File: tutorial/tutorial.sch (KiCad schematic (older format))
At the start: 9 parts

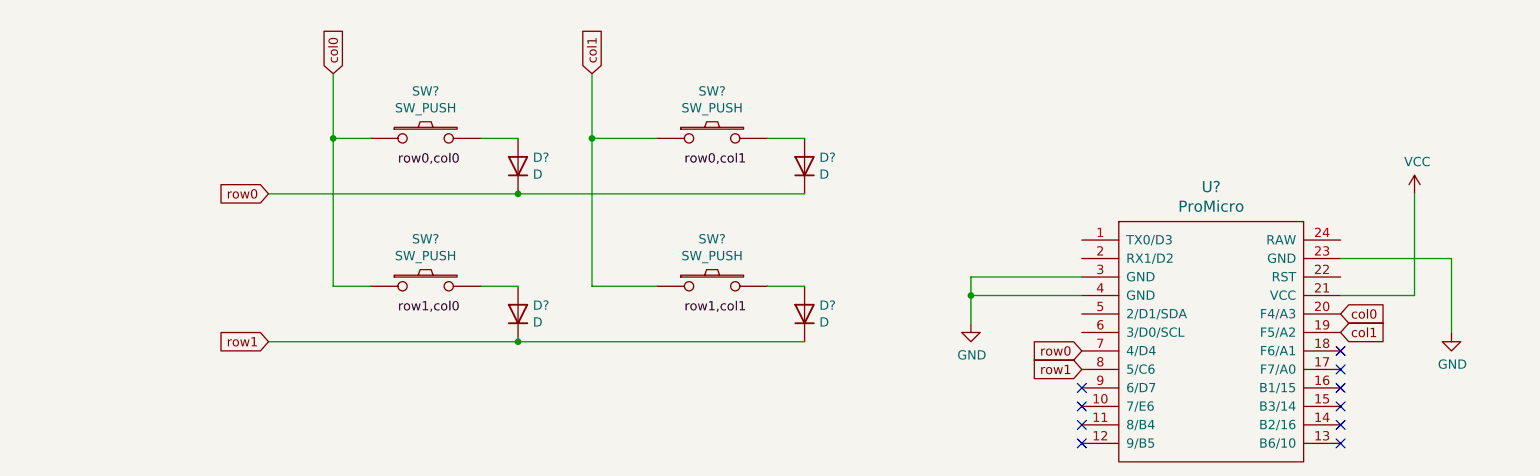
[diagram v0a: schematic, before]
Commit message: [update] リセットスイッチの配置
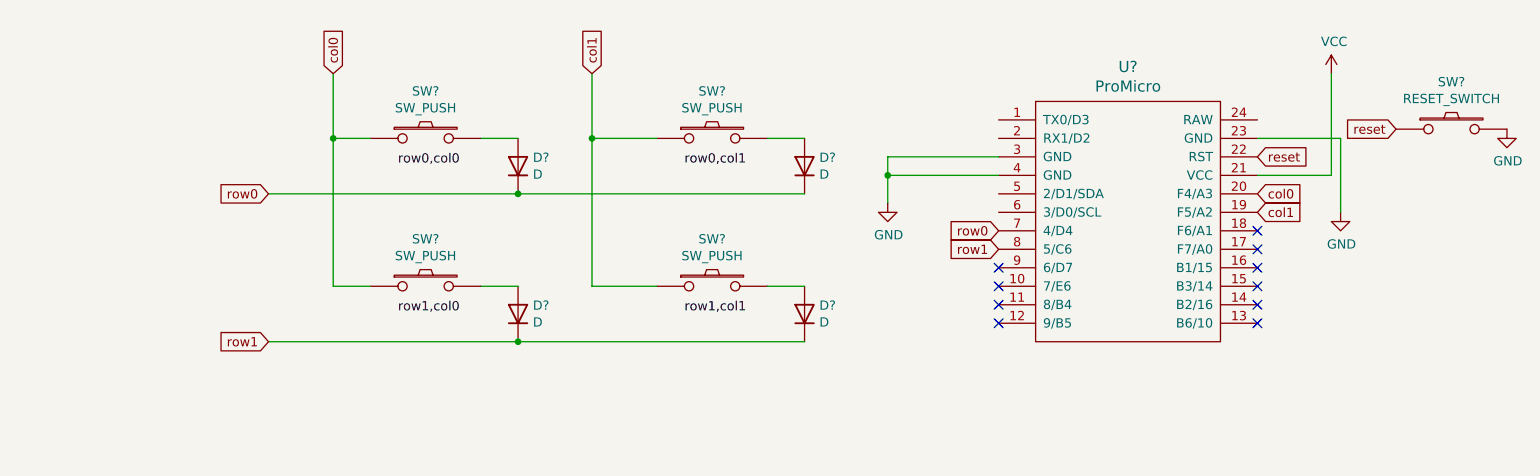
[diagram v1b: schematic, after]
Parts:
- added SW?: RESET_SWITCH, symbol kbd:SW_PUSH
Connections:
- net GND: now also SW?.2
- net reset: now reaches U?.22 (RST)
- net reset: now also SW?.1
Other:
- moved on the sheet: U?
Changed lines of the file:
@@
-$Comp
-L power:GND #PWR?
-U 1 1 62F696F1
-P 10650 2300
-F 0 "#PWR?" H 10650 2050 50  0001 C CNN
-F 1 "GND" H 10655 2127 50  0000 C CNN
-F 2 "" H 10650 2300 50  0001 C CNN
-F 3 "" H 10650 2300 50  0001 C CNN
-	1    10650 2300
-	1    0    0    -1
-$EndComp
 $Comp
 L power:GND #PWR?
 U 1 1 62F6A3B7
-P 8050 2250
-F 0 "#PWR?" H 8050 2000 50  0001 C CNN
-F 1 "GND" H 8055 2077 50  0000 C CNN
-F 2 "" H 8050 2250 50  0001 C CNN
-F 3 "" H 8050 2250 50  0001 C CNN
-	1    8050 2250
+P 7600 1600
+F 0 "#PWR?" H 7600 1350 50  0001 C CNN
+F 1 "GND" H 7605 1427 50  0000 C CNN
+F 2 "" H 7600 1600 50  0001 C CNN
+F 3 "" H 7600 1600 50  0001 C CNN
+	1    7600 1600
 	1    0    0    -1
 $EndComp
@@
 L power:VCC #PWR?
 U 1 1 62F6AAB7
-P 10450 1550
-F 0 "#PWR?" H 10450 1400 50  0001 C CNN
-F 1 "VCC" H 10465 1723 50  0000 C CNN
-F 2 "" H 10450 1550 50  0001 C CNN
-F 3 "" H 10450 1550 50  0001 C CNN
-	1    10450 1550
-	1    0    0    -1
-$EndComp
-Wire Wire Line
-	10050 2100 10450 2100
-Wire Wire Line
-	10450 2100 10450 1550
+P 10000 900
+F 0 "#PWR?" H 10000 750 50  0001 C CNN
+F 1 "VCC" H 10015 1073 50  0000 C CNN
+F 2 "" H 10000 900 50  0001 C CNN
+F 3 "" H 10000 900 50  0001 C CNN
+	1    10000 900
+	1    0    0    -1
+$EndComp
+Wire Wire Line
+	9600 1450 10000 1450
+Wire Wire Line
+	10000 1450 10000 900
 $Comp
 L kbd:ProMicro U?
 U 1 1 62F683C9
-P 9350 2350
-F 0 "U?" H 9350 3187 60  0000 C CNN
-F 1 "ProMicro" H 9350 3081 60  0000 C CNN
-F 2 "" H 9450 1300 60  0000 C CNN
-F 3 "" H 9450 1300 60  0000 C CNN
-	1    9350 2350
-	1    0    0    -1
-$EndComp
-Wire Wire Line
-	10650 2300 10650 1900
-Wire Wire Line
-	10650 1900 10050 1900
-Wire Wire Line
-	8650 2000 8050 2000
-Wire Wire Line
-	8050 2000 8050 2100
-Wire Wire Line
-	8650 2100 8050 2100
-Connection ~ 8050 2100
-Wire Wire Line
-	8050 2100 8050 2250
+P 8900 1700
+F 0 "U?" H 8900 2537 60  0000 C CNN
+F 1 "ProMicro" H 8900 2431 60  0000 C CNN
+F 2 "" H 9000 650 60  0000 C CNN
+F 3 "" H 9000 650 60  0000 C CNN
+	1    8900 1700
+	1    0    0    -1
+$EndComp
+Wire Wire Line
+	10050 1250 9600 1250
+Wire Wire Line
+	8200 1350 7600 1350
+Wire Wire Line
+	7600 1350 7600 1450
+Wire Wire Line
+	8200 1450 7600 1450
+Connection ~ 7600 1450
+Wire Wire Line
+	7600 1450 7600 1600
 $Comp
 L kbd:SW_PUSH SW?
@@
 Text GLabel 4250 2350 0    50   Input ~ 0
 row1
-Text GLabel 10050 2200 2    50   Input ~ 0
+Text GLabel 9600 1550 2    50   Input ~ 0
 col0
-Text GLabel 10050 2300 2    50   Input ~ 0
+Text GLabel 9600 1650 2    50   Input ~ 0
 col1
-Text GLabel 8650 2400 0    50   Input ~ 0
+Text GLabel 8200 1750 0    50   Input ~ 0
 row0
-Text GLabel 8650 2500 0    50   Input ~ 0
+Text GLabel 8200 1850 0    50   Input ~ 0
 row1
-NoConn ~ 10050 2400
-NoConn ~ 10050 2500
-NoConn ~ 10050 2600
-NoConn ~ 10050 2700
-NoConn ~ 10050 2800
-NoConn ~ 10050 2900
-NoConn ~ 8650 2600
-NoConn ~ 8650 2700
-NoConn ~ 8650 2800
-NoConn ~ 8650 2900
+NoConn ~ 9600 1750
+NoConn ~ 9600 1850
+NoConn ~ 9600 1950
+NoConn ~ 9600 2050
+NoConn ~ 9600 2150
+NoConn ~ 9600 2250
+NoConn ~ 8200 1950
+NoConn ~ 8200 2050
+NoConn ~ 8200 2150
+NoConn ~ 8200 2250
+$Comp
+L kbd:SW_PUSH SW?
+U 1 1 62F85B25
+P 10650 1200
+F 0 "SW?" H 10650 1455 50  0000 C CNN
+F 1 "RESET_SWITCH" H 10650 1364 50  0000 C CNN
+F 2 "" H 10650 1200 50  0000 C CNN
+F 3 "" H 10650 1200 50  0000 C CNN
+	1    10650 1200
+	1    0    0    -1
+$EndComp
+$Comp
+L power:GND #PWR?
+U 1 1 62F880C9
+P 10950 1200
+F 0 "#PWR?" H 10950 950 50  0001 C CNN
+F 1 "GND" H 10955 1027 50  0000 C CNN
+F 2 "" H 10950 1200 50  0001 C CNN
+F 3 "" H 10950 1200 50  0001 C CNN
+	1    10950 1200
+	1    0    0    -1
+$EndComp
+Text GLabel 10350 1200 0    50   Input ~ 0
+reset
+Wire Wire Line
+	10050 1650 10050 1250
+$Comp
+L power:GND #PWR?
+U 1 1 62F696F1
+P 10050 1650
+F 0 "#PWR?" H 10050 1400 50  0001 C CNN
+F 1 "GND" H 10055 1477 50  0000 C CNN
+F 2 "" H 10050 1650 50  0001 C CNN
+F 3 "" H 10050 1650 50  0001 C CNN
+	1    10050 1650
+	1    0    0    -1
+$EndComp
+Text GLabel 9600 1350 2    50   Input ~ 0
+reset
 $EndSCHEMATC

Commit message: [update] TRRSジャックの配置とPWR_FLAGの定義
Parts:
- added J?: MJ-4PP-9, symbol kbd:MJ-4PP-9
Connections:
- net GND: now also J?.C
- net VCC: now also J?.D
- net led: now reaches U?.1 (TX0/D3)
- net data: now reaches U?.2 (RX1/D2)
- net data: now also J?.B
- no-connect marks 10 -> 11
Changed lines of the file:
@@
 Text GLabel 9600 1350 2    50   Input ~ 0
 reset
+$Comp
+L kbd:MJ-4PP-9 J?
+U 1 1 62F920CE
+P 3075 1250
+F 0 "J?" H 3106 1526 50  0000 C CNN
+F 1 "MJ-4PP-9" H 3106 1435 50  0000 C CNN
+F 2 "" H 3350 1425 50  0001 C CNN
+F 3 "~" H 3350 1425 50  0001 C CNN
+	1    3075 1250
+	1    0    0    -1
+$EndComp
+$Comp
+L power:VCC #PWR?
+U 1 1 62F95D7E
+P 3400 1000
+F 0 "#PWR?" H 3400 850 50  0001 C CNN
+F 1 "VCC" H 3415 1173 50  0000 C CNN
+F 2 "" H 3400 1000 50  0001 C CNN
+F 3 "" H 3400 1000 50  0001 C CNN
+	1    3400 1000
+	1    0    0    -1
+$EndComp
+$Comp
+L power:GND #PWR?
+U 1 1 62F96C77
+P 3400 1550
+F 0 "#PWR?" H 3400 1300 50  0001 C CNN
+F 1 "GND" H 3405 1377 50  0000 C CNN
+F 2 "" H 3400 1550 50  0001 C CNN
+F 3 "" H 3400 1550 50  0001 C CNN
+	1    3400 1550
+	1    0    0    -1
+$EndComp
+Wire Wire Line
+	3400 1000 3400 1225
+Wire Wire Line
+	3400 1225 3275 1225
+Wire Wire Line
+	3275 1275 3400 1275
+Wire Wire Line
+	3400 1275 3400 1550
+Text GLabel 3550 1325 2    50   Input ~ 0
+data
+Wire Wire Line
+	3550 1325 3275 1325
+NoConn ~ 3275 1175
+Text GLabel 8200 1250 0    50   Input ~ 0
+data
+Text GLabel 8200 1150 0    50   Input ~ 0
+led
+$Comp
+L power:GND #PWR?
+U 1 1 62FA2F38
+P 3800 850
+F 0 "#PWR?" H 3800 600 50  0001 C CNN
+F 1 "GND" H 3805 677 50  0000 C CNN
+F 2 "" H 3800 850 50  0001 C CNN
+F 3 "" H 3800 850 50  0001 C CNN
+	1    3800 850
+	1    0    0    -1
+$EndComp
+$Comp
+L power:VCC #PWR?
+U 1 1 62FA3341
+P 4100 850
+F 0 "#PWR?" H 4100 700 50  0001 C CNN
+F 1 "VCC" H 4115 1023 50  0000 C CNN
+F 2 "" H 4100 850 50  0001 C CNN
+F 3 "" H 4100 850 50  0001 C CNN
+	1    4100 850
+	1    0    0    -1
+$EndComp
+$Comp
+L power:PWR_FLAG #FLG?
+U 1 1 62FA43DF
+P 3800 850
+F 0 "#FLG?" H 3800 925 50  0001 C CNN
+F 1 "PWR_FLAG" H 3800 1023 50  0000 C CNN
+F 2 "" H 3800 850 50  0001 C CNN
+F 3 "~" H 3800 850 50  0001 C CNN
+	1    3800 850
+	1    0    0    -1
+$EndComp
+$Comp
+L power:PWR_FLAG #FLG?
+U 1 1 62FA502D
+P 4100 850
+F 0 "#FLG?" H 4100 925 50  0001 C CNN
+F 1 "PWR_FLAG" H 4100 1023 50  0000 C CNN
+F 2 "" H 4100 850 50  0001 C CNN
+F 3 "~" H 4100 850 50  0001 C CNN
+	1    4100 850
+	-1   0    0    1
+$EndComp
 $EndSCHEMATC

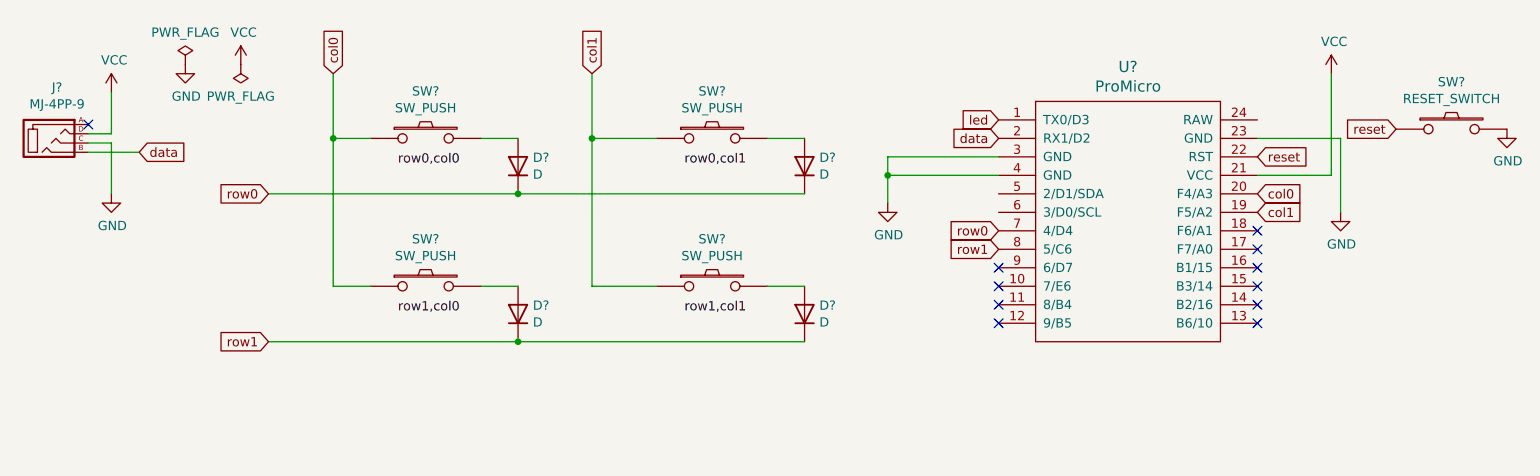
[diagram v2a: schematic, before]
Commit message: [add] LEDシンボルの追加とアノテーションとルールチェックの実行
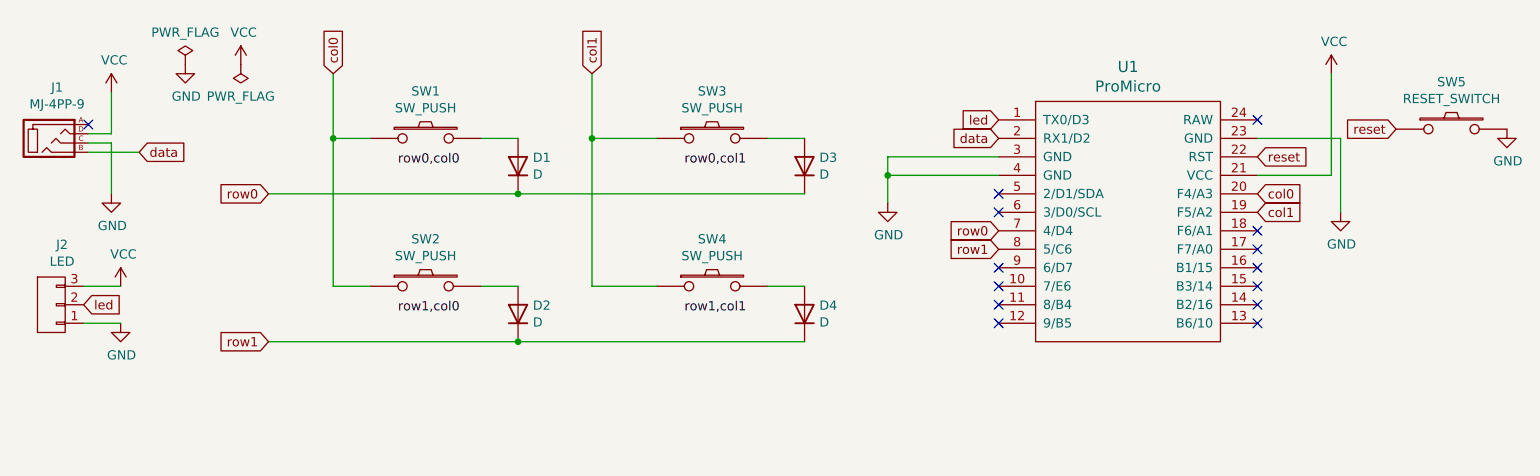
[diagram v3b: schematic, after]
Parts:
- added J2: LED, symbol kibou-kbd:LED
- gave numbers to parts that had none: 11
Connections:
- net GND: now also J2.1
- net VCC: now also J2.3
- net led: now also J2.2
- no-connect marks 11 -> 14
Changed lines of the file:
@@
 $EndDescr
 $Comp
-L power:GND #PWR?
+L power:GND #PWR05
 U 1 1 62F6A3B7
 P 7600 1600
-F 0 "#PWR?" H 7600 1350 50  0001 C CNN
+F 0 "#PWR05" H 7600 1350 50  0001 C CNN
 F 1 "GND" H 7605 1427 50  0000 C CNN
 F 2 "" H 7600 1600 50  0001 C CNN
@@
 $EndComp
 $Comp
-L power:VCC #PWR?
+L power:VCC #PWR06
 U 1 1 62F6AAB7
 P 10000 900
-F 0 "#PWR?" H 10000 750 50  0001 C CNN
+F 0 "#PWR06" H 10000 750 50  0001 C CNN
 F 1 "VCC" H 10015 1073 50  0000 C CNN
 F 2 "" H 10000 900 50  0001 C CNN
@@
 	10000 1450 10000 900
 $Comp
-L kbd:ProMicro U?
+L kbd:ProMicro U1
 U 1 1 62F683C9
 P 8900 1700
-F 0 "U?" H 8900 2537 60  0000 C CNN
+F 0 "U1" H 8900 2537 60  0000 C CNN
 F 1 "ProMicro" H 8900 2431 60  0000 C CNN
 F 2 "" H 9000 650 60  0000 C CNN
@@
 	7600 1450 7600 1600
 $Comp
-L kbd:SW_PUSH SW?
+L kbd:SW_PUSH SW3
 U 1 1 62F75EFC
 P 6650 1250
-F 0 "SW?" H 6650 1505 50  0000 C CNN
+F 0 "SW3" H 6650 1505 50  0000 C CNN
 F 1 "SW_PUSH" H 6650 1414 50  0000 C CNN
 F 2 "" H 6650 1250 50  0000 C CNN
@@
 $EndComp
 $Comp
-L kbd:SW_PUSH SW?
+L kbd:SW_PUSH SW4
 U 1 1 62F7645F
 P 6650 2050
-F 0 "SW?" H 6650 2305 50  0000 C CNN
+F 0 "SW4" H 6650 2305 50  0000 C CNN
 F 1 "SW_PUSH" H 6650 2214 50  0000 C CNN
 F 2 "" H 6650 2050 50  0000 C CNN
@@
 $EndComp
 $Comp
-L kbd:SW_PUSH SW?
+L kbd:SW_PUSH SW2
 U 1 1 62F761DE
 P 5100 2050
-F 0 "SW?" H 5100 2305 50  0000 C CNN
+F 0 "SW2" H 5100 2305 50  0000 C CNN
 F 1 "SW_PUSH" H 5100 2214 50  0000 C CNN
 F 2 "" H 5100 2050 50  0000 C CNN
@@
 $EndComp
 $Comp
-L kbd:SW_PUSH SW?
+L kbd:SW_PUSH SW1
 U 1 1 62F741D1
 P 5100 1250
-F 0 "SW?" H 5100 1505 50  0000 C CNN
+F 0 "SW1" H 5100 1505 50  0000 C CNN
 F 1 "SW_PUSH" H 5100 1414 50  0000 C CNN
 F 2 "" H 5100 1250 50  0000 C CNN
@@
 	6350 1250 6000 1250
 $Comp
-L Device:D D?
+L Device:D D3
 U 1 1 62F7A838
 P 7150 1400
-F 0 "D?" V 7196 1320 50  0000 R CNN
+F 0 "D3" V 7196 1320 50  0000 R CNN
 F 1 "D" V 7105 1320 50  0000 R CNN
 F 2 "" H 7150 1400 50  0001 C CNN
@@
 $EndComp
 $Comp
-L Device:D D?
+L Device:D D4
 U 1 1 62F7D52A
 P 7150 2200
-F 0 "D?" V 7196 2120 50  0000 R CNN
+F 0 "D4" V 7196 2120 50  0000 R CNN
 F 1 "D" V 7105 2120 50  0000 R CNN
 F 2 "" H 7150 2200 50  0001 C CNN
@@
 $EndComp
 $Comp
-L Device:D D?
+L Device:D D2
 U 1 1 62F7E030
 P 5600 2200
-F 0 "D?" V 5646 2120 50  0000 R CNN
+F 0 "D2" V 5646 2120 50  0000 R CNN
 F 1 "D" V 5555 2120 50  0000 R CNN
 F 2 "" H 5600 2200 50  0001 C CNN
@@
 $EndComp
 $Comp
-L Device:D D?
+L Device:D D1
 U 1 1 62F7E5E0
 P 5600 1400
-F 0 "D?" V 5646 1320 50  0000 R CNN
+F 0 "D1" V 5646 1320 50  0000 R CNN
 F 1 "D" V 5555 1320 50  0000 R CNN
 F 2 "" H 5600 1400 50  0001 C CNN
@@
 NoConn ~ 8200 2250
 $Comp
-L kbd:SW_PUSH SW?
+L kbd:SW_PUSH SW5
 U 1 1 62F85B25
 P 10650 1200
-F 0 "SW?" H 10650 1455 50  0000 C CNN
+F 0 "SW5" H 10650 1455 50  0000 C CNN
 F 1 "RESET_SWITCH" H 10650 1364 50  0000 C CNN
 F 2 "" H 10650 1200 50  0000 C CNN
@@
 $EndComp
 $Comp
-L power:GND #PWR?
+L power:GND #PWR08
 U 1 1 62F880C9
 P 10950 1200
-F 0 "#PWR?" H 10950 950 50  0001 C CNN
+F 0 "#PWR08" H 10950 950 50  0001 C CNN
 F 1 "GND" H 10955 1027 50  0000 C CNN
 F 2 "" H 10950 1200 50  0001 C CNN
@@
 	10050 1650 10050 1250
 $Comp
-L power:GND #PWR?
+L power:GND #PWR07
 U 1 1 62F696F1
 P 10050 1650
-F 0 "#PWR?" H 10050 1400 50  0001 C CNN
+F 0 "#PWR07" H 10050 1400 50  0001 C CNN
 F 1 "GND" H 10055 1477 50  0000 C CNN
 F 2 "" H 10050 1650 50  0001 C CNN
@@
 reset
 $Comp
-L kbd:MJ-4PP-9 J?
+L kbd:MJ-4PP-9 J1
 U 1 1 62F920CE
 P 3075 1250
-F 0 "J?" H 3106 1526 50  0000 C CNN
+F 0 "J1" H 3106 1526 50  0000 C CNN
 F 1 "MJ-4PP-9" H 3106 1435 50  0000 C CNN
 F 2 "" H 3350 1425 50  0001 C CNN
@@
 $EndComp
 $Comp
-L power:VCC #PWR?
+L power:VCC #PWR01
 U 1 1 62F95D7E
 P 3400 1000
-F 0 "#PWR?" H 3400 850 50  0001 C CNN
+F 0 "#PWR01" H 3400 850 50  0001 C CNN
 F 1 "VCC" H 3415 1173 50  0000 C CNN
 F 2 "" H 3400 1000 50  0001 C CNN
@@
 $EndComp
 $Comp
-L power:GND #PWR?
+L power:GND #PWR02
 U 1 1 62F96C77
 P 3400 1550
-F 0 "#PWR?" H 3400 1300 50  0001 C CNN
+F 0 "#PWR02" H 3400 1300 50  0001 C CNN
 F 1 "GND" H 3405 1377 50  0000 C CNN
 F 2 "" H 3400 1550 50  0001 C CNN
@@
 Text GLabel 8200 1250 0    50   Input ~ 0
 data
-Text GLabel 8200 1150 0    50   Input ~ 0
-led
-$Comp
-L power:GND #PWR?
+$Comp
+L power:GND #PWR03
 U 1 1 62FA2F38
 P 3800 850
-F 0 "#PWR?" H 3800 600 50  0001 C CNN
+F 0 "#PWR03" H 3800 600 50  0001 C CNN
 F 1 "GND" H 3805 677 50  0000 C CNN
 F 2 "" H 3800 850 50  0001 C CNN
@@
 $EndComp
 $Comp
-L power:VCC #PWR?
+L power:VCC #PWR04
 U 1 1 62FA3341
 P 4100 850
-F 0 "#PWR?" H 4100 700 50  0001 C CNN
+F 0 "#PWR04" H 4100 700 50  0001 C CNN
 F 1 "VCC" H 4115 1023 50  0000 C CNN
 F 2 "" H 4100 850 50  0001 C CNN
@@
 $EndComp
 $Comp
-L power:PWR_FLAG #FLG?
+L power:PWR_FLAG #FLG01
 U 1 1 62FA43DF
 P 3800 850
-F 0 "#FLG?" H 3800 925 50  0001 C CNN
+F 0 "#FLG01" H 3800 925 50  0001 C CNN
 F 1 "PWR_FLAG" H 3800 1023 50  0000 C CNN
 F 2 "" H 3800 850 50  0001 C CNN
@@
 $EndComp
 $Comp
-L power:PWR_FLAG #FLG?
+L power:PWR_FLAG #FLG02
 U 1 1 62FA502D
 P 4100 850
-F 0 "#FLG?" H 4100 925 50  0001 C CNN
+F 0 "#FLG02" H 4100 925 50  0001 C CNN
 F 1 "PWR_FLAG" H 4100 1023 50  0000 C CNN
 F 2 "" H 4100 850 50  0001 C CNN
@@
 	-1   0    0    1
 $EndComp
+NoConn ~ 9600 1150
+NoConn ~ 8200 1550
+NoConn ~ 8200 1650
+$Comp
+L kibou-kbd:LED J2
+U 1 1 62FAE5A9
+P 3100 2050
+F 0 "J2" H 3133 2275 50  0000 C CNN
+F 1 "LED" H 3133 2184 50  0000 C CNN
+F 2 "" H 3100 2250 50  0001 C CNN
+F 3 "" H 3100 2250 50  0001 C CNN
+	1    3100 2050
+	1    0    0    -1
+$EndComp
+Text GLabel 3250 2150 2    50   Input ~ 0
+led
+$Comp
+L power:VCC #PWR09
+U 1 1 62FB05F9
+P 3450 2050
+F 0 "#PWR09" H 3450 1900 50  0001 C CNN
+F 1 "VCC" H 3465 2223 50  0000 C CNN
+F 2 "" H 3450 2050 50  0001 C CNN
+F 3 "" H 3450 2050 50  0001 C CNN
+	1    3450 2050
+	1    0    0    -1
+$EndComp
+$Comp
+L power:GND #PWR010
+U 1 1 62FB0FF7
+P 3450 2250
+F 0 "#PWR010" H 3450 2000 50  0001 C CNN
+F 1 "GND" H 3455 2077 50  0000 C CNN
+F 2 "" H 3450 2250 50  0001 C CNN
+F 3 "" H 3450 2250 50  0001 C CNN
+	1    3450 2250
+	1    0    0    -1
+$EndComp
+Wire Wire Line
+	3250 2250 3450 2250
+Wire Wire Line
+	3250 2050 3450 2050
+Text GLabel 8200 1150 0    50   Input ~ 0
+led
 $EndSCHEMATC
